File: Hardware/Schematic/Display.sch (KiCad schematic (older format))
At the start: 16 parts, among them J8 Conn_01x24

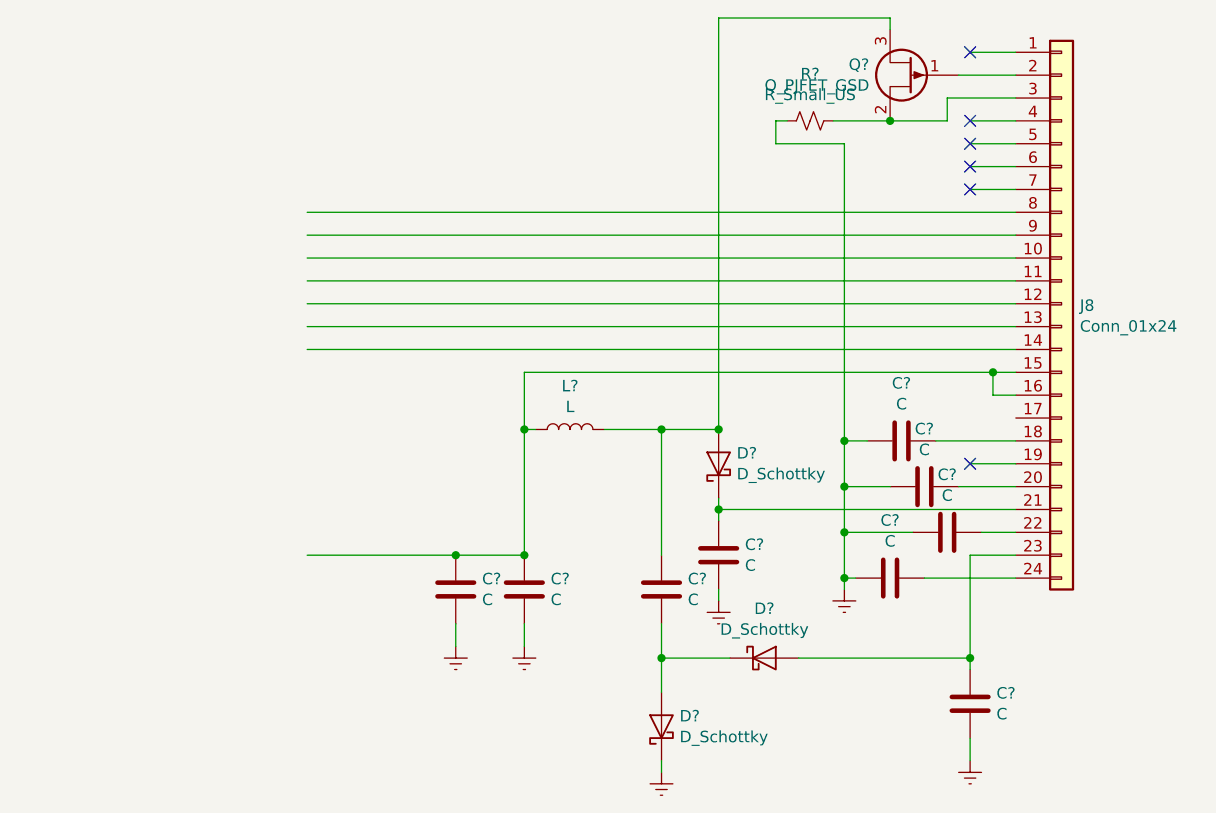
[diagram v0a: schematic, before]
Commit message: Lots of schematic updates
Lots of stuff...

* Added a new 8-pin TVS diode array
* Finalized the display connector
* Corrected the net labels to global labels so they span across sheets
* Added a 5V linear voltage regulator and LEDs to debug power
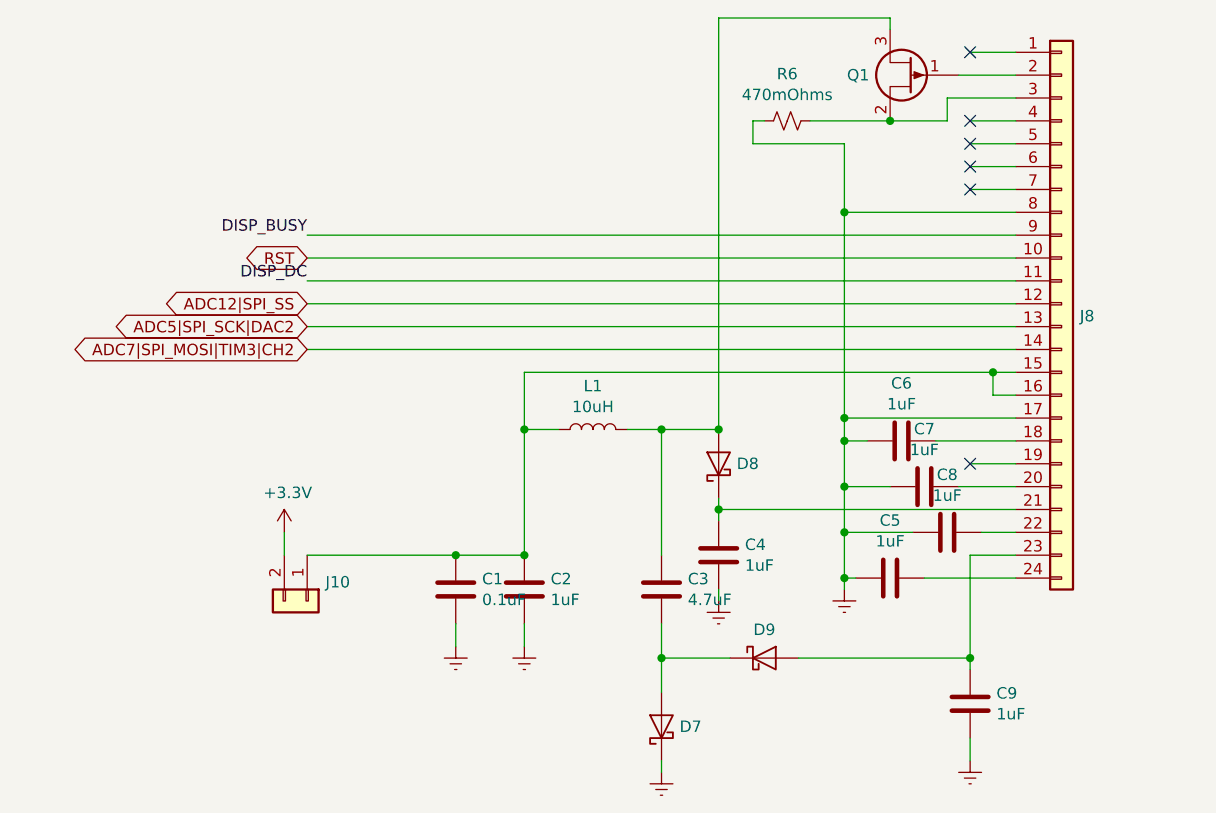
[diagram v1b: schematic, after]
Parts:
- added J10: Conn_01x02, Connector_PinHeader_2.54mm:PinHeader_1x02_P2.54mm_Vertical, symbol Connector_Generic:Conn_01x02
- C1: renamed from C?; value C -> 0.1uF; footprint (none) -> Capacitor_SMD:C_2512_6332Metric_Pad1.52x3.35mm_HandSolder
- C2, C4, C5, C6, C7, C8, C9: renamed from C?; value C -> 1uF; footprint (none) -> Capacitor_SMD:C_2512_6332Metric_Pad1.52x3.35mm_HandSolder
- C3: renamed from C?; value C -> 4.7uF; footprint (none) -> Capacitor_SMD:C_2512_6332Metric_Pad1.52x3.35mm_HandSolder
- D7, D8, D9: renamed from D?; footprint (none) -> Diode_SMD:D_2512_6332Metric_Pad1.52x3.35mm_HandSolder
- L1: renamed from L?; value L -> 10uH; footprint (none) -> Inductor_SMD:L_2512_6332Metric_Pad1.52x3.35mm_HandSolder
- Q1: renamed from Q?; footprint (none) -> Package_TO_SOT_SMD:SOT-23
- R6: renamed from R?; value R_Small_US -> 470mOhms; footprint (none) -> Resistor_SMD:R_2512_6332Metric_Pad1.52x3.35mm_HandSolder
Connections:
- net labels added: +3.3V, ADC12|SPI_SS, ADC5|SPI_SCK|DAC2, ADC7|SPI_MOSI|TIM3|CH2, DISP_BUSY, DISP_DC, RST
- wire segments 64 -> 68
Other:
- moved on the sheet: L1, R6
